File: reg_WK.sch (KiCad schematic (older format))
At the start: 32 parts, among them U36 74HC373, U37 74HC373, U38 74HC244, U39 74HC244, U40 74HC244, U41 74HC244

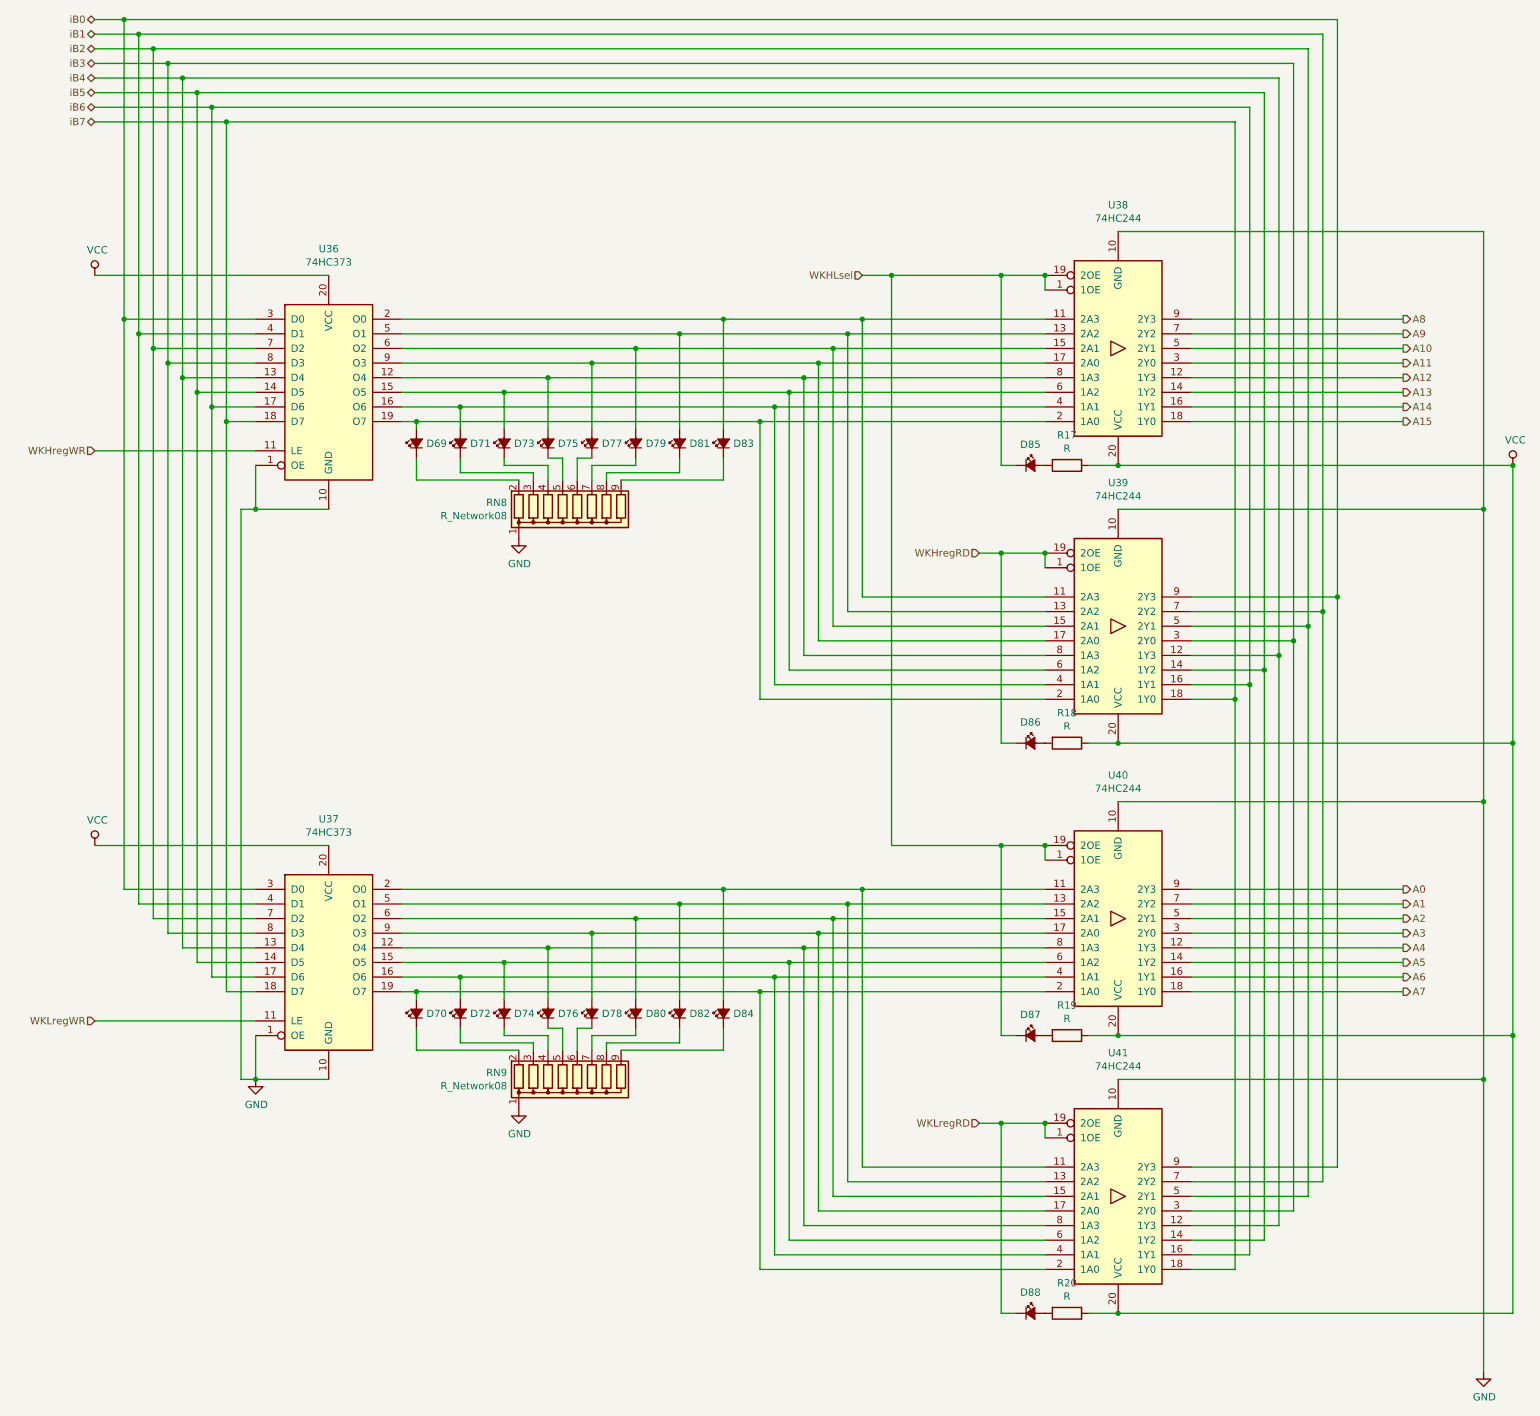
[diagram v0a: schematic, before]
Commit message: placed WKL register, start routing
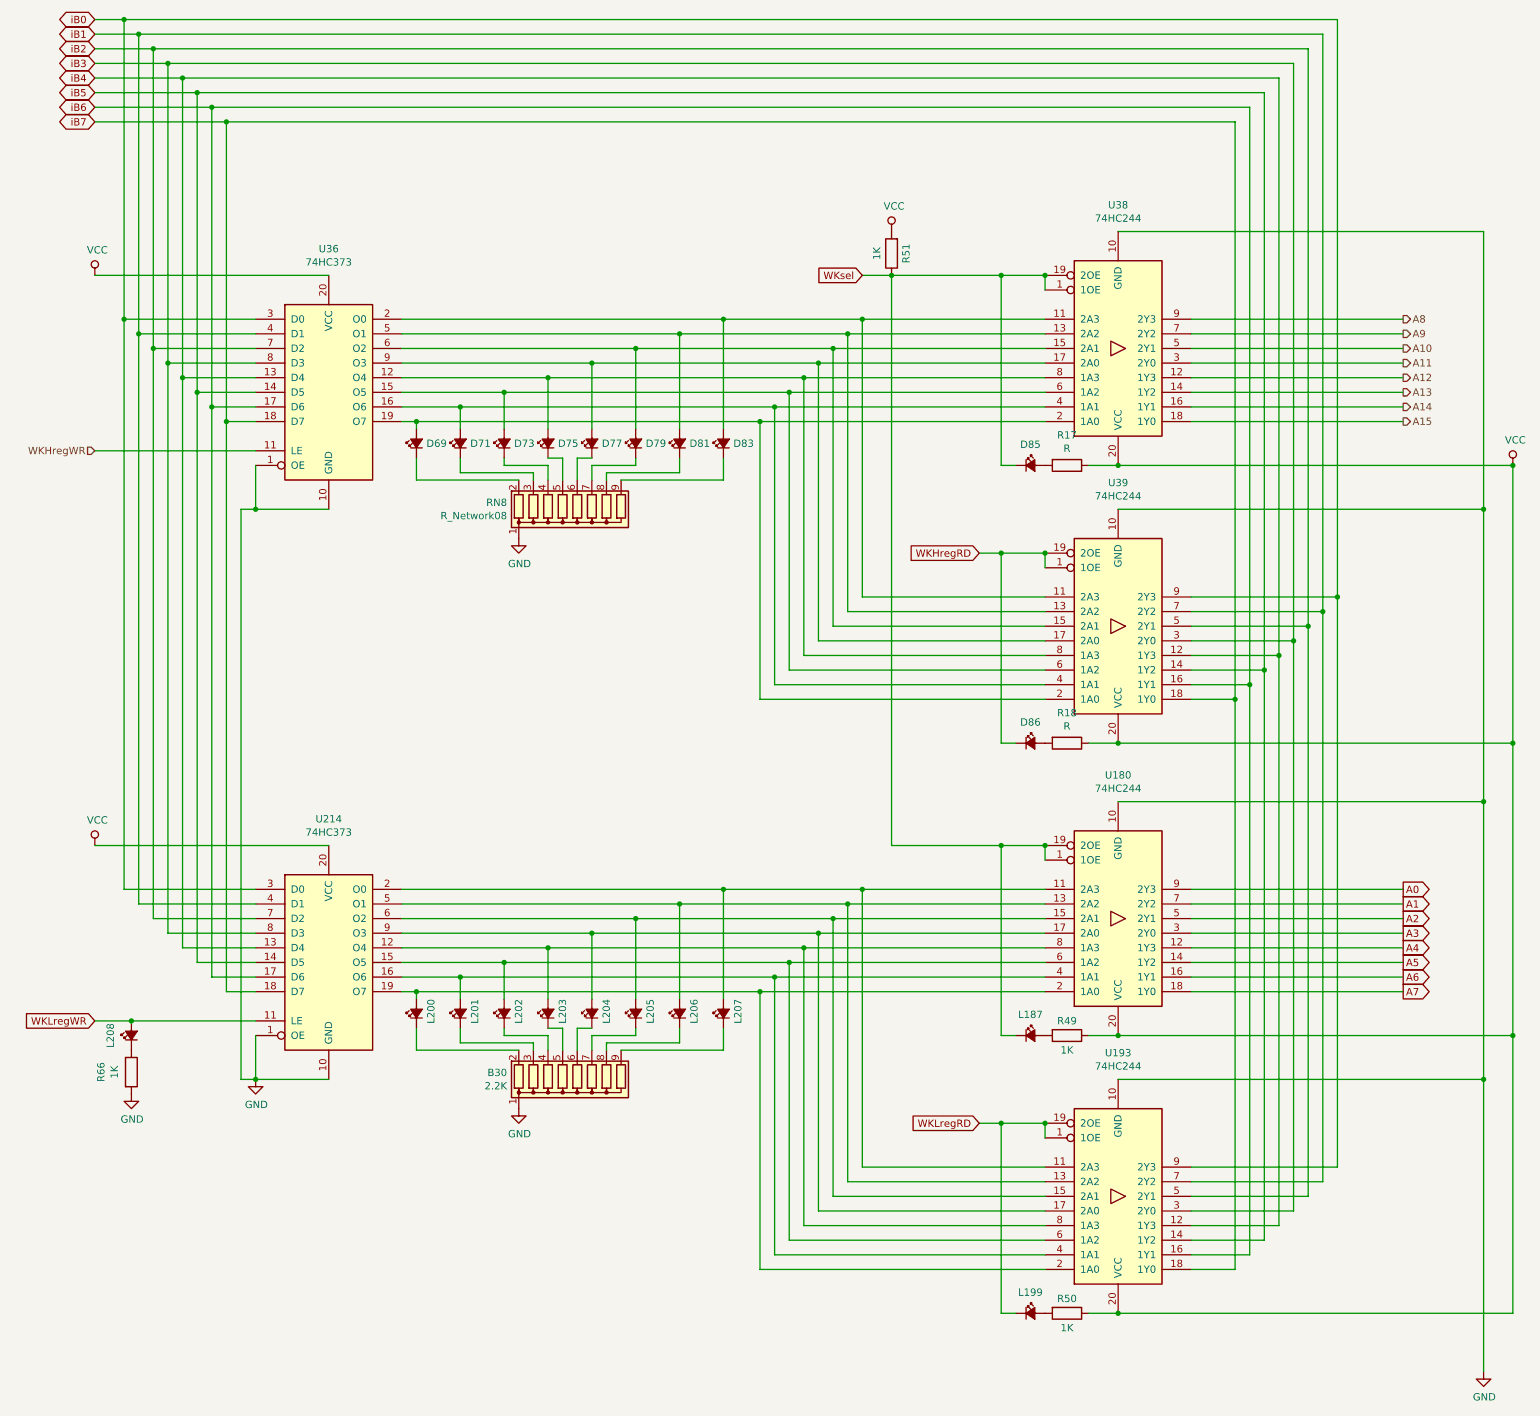
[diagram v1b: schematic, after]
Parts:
- added L208: LED_Small_ALT, LED_THT:LED_D3.0mm, symbol Device:LED_Small_ALT
- added R51, R66: 1K, Resistor_THT:R_Axial_DIN0207_L6.3mm_D2.5mm_P10.16mm_Horizontal, symbol Device:R
- B30: renamed from RN9; value R_Network08 -> 2.2K
- R49: renamed from R19; value R -> 1K
- R50: renamed from R20; value R -> 1K
- renumbered D87 to L187, D88 to L199, D70 to L200, D72 to L201, D74 to L202, D76 to L203, D78 to L204, D80 to L205, D82 to L206, D84 to L207, U40 to U180, U41 to U193, U37 to U214
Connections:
- net GND: now also R66.2
- net VCC: now also R51.2
- net WKLregWR: now also L208.2 (A)
- net WKHLsel renamed WKsel
- net WKsel: now also R51.1
- new net: L208.1 (K), R66.1

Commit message: oops, had to redo part of the PC because I inverted U182 and U195, also routed A0-A7 through the PC register
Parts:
- R49, R50, R51, R66: footprint Resistor_THT:R_Axial_DIN0207_L6.3mm_D2.5mm_P10.16mm_Horizontal -> Resistor_THT:R_Axial_DIN0204_L3.6mm_D1.6mm_P5.08mm_Horizontal
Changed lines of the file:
@@
 F 0 "R49" V 7950 8100 50  0000 C CNN
 F 1 "1K" V 8150 8100 50  0000 C CNN
-F 2 "Resistor_THT:R_Axial_DIN0207_L6.3mm_D2.5mm_P10.16mm_Horizontal" V 7980 8100 50  0001 C CNN
+F 2 "Resistor_THT:R_Axial_DIN0204_L3.6mm_D1.6mm_P5.08mm_Horizontal" V 7980 8100 50  0001 C CNN
 F 3 "~" H 8050 8100 50  0001 C CNN
 	1    8050 8100
@@
 F 0 "R50" V 7950 10000 50  0000 C CNN
 F 1 "1K" V 8150 10000 50  0000 C CNN
-F 2 "Resistor_THT:R_Axial_DIN0207_L6.3mm_D2.5mm_P10.16mm_Horizontal" V 7980 10000 50  0001 C CNN
+F 2 "Resistor_THT:R_Axial_DIN0204_L3.6mm_D1.6mm_P5.08mm_Horizontal" V 7980 10000 50  0001 C CNN
 F 3 "~" H 8050 10000 50  0001 C CNN
 	1    8050 10000
@@
 F 0 "R66" V 1443 8350 50  0000 C CNN
 F 1 "1K" V 1534 8350 50  0000 C CNN
-F 2 "Resistor_THT:R_Axial_DIN0207_L6.3mm_D2.5mm_P10.16mm_Horizontal" V 1580 8350 50  0001 C CNN
+F 2 "Resistor_THT:R_Axial_DIN0204_L3.6mm_D1.6mm_P5.08mm_Horizontal" V 1580 8350 50  0001 C CNN
 F 3 "~" H 1650 8350 50  0001 C CNN
 	1    1650 8350
@@
 P 1650 8500
 AR Path="/5D8315BB/5CFE7E22" Ref="#PWR?"  Part="1"
-AR Path="/5E045D26/5CFE7E22" Ref="#PWR?"  Part="1"
-F 0 "#PWR?" H 1650 8250 50  0001 C CNN
+AR Path="/5E045D26/5CFE7E22" Ref="#PWR0205"  Part="1"
+F 0 "#PWR0205" H 1650 8250 50  0001 C CNN
 F 1 "GND" H 1655 8327 50  0000 C CNN
 F 2 "" H 1650 8500 50  0001 C CNN
@@
 F 0 "R51" V 6750 2750 50  0000 C CNN
 F 1 "1K" V 6950 2750 50  0000 C CNN
-F 2 "Resistor_THT:R_Axial_DIN0207_L6.3mm_D2.5mm_P10.16mm_Horizontal" V 6780 2750 50  0001 C CNN
+F 2 "Resistor_THT:R_Axial_DIN0204_L3.6mm_D1.6mm_P5.08mm_Horizontal" V 6780 2750 50  0001 C CNN
 F 3 "~" H 6850 2750 50  0001 C CNN
 	1    6850 2750
@@
 AR Path="/5D8315BB/5D001AE2" Ref="#PWR?"  Part="1"
 AR Path="/5E031B2C/5D001AE2" Ref="#PWR?"  Part="1"
-AR Path="/5E045D26/5D001AE2" Ref="#PWR?"  Part="1"
-F 0 "#PWR?" H 6850 2450 50  0001 C CNN
+AR Path="/5E045D26/5D001AE2" Ref="#PWR0206"  Part="1"
+F 0 "#PWR0206" H 6850 2450 50  0001 C CNN
 F 1 "VCC" H 6867 2773 50  0000 C CNN
 F 2 "" H 6850 2600 50  0001 C CNN

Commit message: route part of A8-A15 from WKL to WKH
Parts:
- removed D85: LED_Small_ALT, LED_THT:LED_D3.0mm, symbol Device:LED_Small_ALT
- removed R17: R, Resistor_THT:R_Axial_DIN0207_L6.3mm_D2.5mm_P10.16mm_Horizontal, symbol Device:R
- added L198: LED_Small_ALT, LED_THT:LED_D3.0mm, symbol Device:LED_Small_ALT
- added R65: 1K, Resistor_THT:R_Axial_DIN0204_L3.6mm_D1.6mm_P5.08mm_Horizontal, symbol Device:R
- B29: renamed from RN8; value R_Network08 -> 2.2K
- R64: renamed from R18; value R -> 1K; footprint Resistor_THT:R_Axial_DIN0207_L6.3mm_D2.5mm_P10.16mm_Horizontal -> Resistor_THT:R_Axial_DIN0204_L3.6mm_D1.6mm_P5.08mm_Horizontal
- renumbered D86 to L189, D83 to L190, D81 to L191, D79 to L192, D77 to L193, D75 to L194, D73 to L195, D71 to L196, D69 to L197, U38 to U179, U39 to U192, U36 to U213
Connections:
- net GND: now also R65.2
- net WKHregWR: now also L198.2 (A)
- new net: L198.1 (K), R65.1
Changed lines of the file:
@@
 AR Path="/5D8315BB/5E39B533" Ref="U?"  Part="1"
 AR Path="/5E031B2C/5E39B533" Ref="U?"  Part="1"
-AR Path="/5E045D26/5E39B533" Ref="U36"  Part="1"
-F 0 "U36" H 3000 4681 50  0000 C CNN
+AR Path="/5E045D26/5E39B533" Ref="U213"  Part="1"
+F 0 "U213" H 3000 4681 50  0000 C CNN
 F 1 "74HC373" H 3000 4590 50  0000 C CNN
 F 2 "Package_DIP:DIP-20_W7.62mm" H 3000 3700 50  0001 C CNN
@@
 	1    0    0    -1
 $EndComp
-Text HLabel 1400 4100 0    50   Input ~ 0
-WKHregWR
 $Comp
 L Device:LED_Small_ALT D?
@@
 AR Path="/5D8315BB/5E39B55B" Ref="D?"  Part="1"
 AR Path="/5E031B2C/5E39B55B" Ref="D?"  Part="1"
-AR Path="/5E045D26/5E39B55B" Ref="D69"  Part="1"
-F 0 "D69" V 3600 3982 50  0000 R CNN
+AR Path="/5E045D26/5E39B55B" Ref="L197"  Part="1"
+F 0 "L197" V 3600 3982 50  0000 R CNN
 F 1 "LED_Small_ALT" V 3555 3982 50  0001 R CNN
 F 2 "LED_THT:LED_D3.0mm" V 3600 4050 50  0001 C CNN
@@
 AR Path="/5D8315BB/5E39B561" Ref="D?"  Part="1"
 AR Path="/5E031B2C/5E39B561" Ref="D?"  Part="1"
-AR Path="/5E045D26/5E39B561" Ref="D71"  Part="1"
-F 0 "D71" V 3900 3982 50  0000 R CNN
+AR Path="/5E045D26/5E39B561" Ref="L196"  Part="1"
+F 0 "L196" V 3900 3982 50  0000 R CNN
 F 1 "LED_Small_ALT" V 3855 3982 50  0001 R CNN
 F 2 "LED_THT:LED_D3.0mm" V 3900 4050 50  0001 C CNN
@@
 AR Path="/5D8315BB/5E39B567" Ref="D?"  Part="1"
 AR Path="/5E031B2C/5E39B567" Ref="D?"  Part="1"
-AR Path="/5E045D26/5E39B567" Ref="D73"  Part="1"
-F 0 "D73" V 4200 3982 50  0000 R CNN
+AR Path="/5E045D26/5E39B567" Ref="L195"  Part="1"
+F 0 "L195" V 4200 3982 50  0000 R CNN
 F 1 "LED_Small_ALT" V 4155 3982 50  0001 R CNN
 F 2 "LED_THT:LED_D3.0mm" V 4200 4050 50  0001 C CNN
@@
 AR Path="/5D8315BB/5E39B56D" Ref="D?"  Part="1"
 AR Path="/5E031B2C/5E39B56D" Ref="D?"  Part="1"
-AR Path="/5E045D26/5E39B56D" Ref="D75"  Part="1"
-F 0 "D75" V 4500 3982 50  0000 R CNN
+AR Path="/5E045D26/5E39B56D" Ref="L194"  Part="1"
+F 0 "L194" V 4500 3982 50  0000 R CNN
 F 1 "LED_Small_ALT" V 4455 3982 50  0001 R CNN
 F 2 "LED_THT:LED_D3.0mm" V 4500 4050 50  0001 C CNN
@@
 AR Path="/5D8315BB/5E39B573" Ref="D?"  Part="1"
 AR Path="/5E031B2C/5E39B573" Ref="D?"  Part="1"
-AR Path="/5E045D26/5E39B573" Ref="D77"  Part="1"
-F 0 "D77" V 4800 3982 50  0000 R CNN
+AR Path="/5E045D26/5E39B573" Ref="L193"  Part="1"
+F 0 "L193" V 4800 3982 50  0000 R CNN
 F 1 "LED_Small_ALT" V 4755 3982 50  0001 R CNN
 F 2 "LED_THT:LED_D3.0mm" V 4800 4050 50  0001 C CNN
@@
 AR Path="/5D8315BB/5E39B579" Ref="D?"  Part="1"
 AR Path="/5E031B2C/5E39B579" Ref="D?"  Part="1"
-AR Path="/5E045D26/5E39B579" Ref="D79"  Part="1"
-F 0 "D79" V 5100 3982 50  0000 R CNN
+AR Path="/5E045D26/5E39B579" Ref="L192"  Part="1"
+F 0 "L192" V 5100 3982 50  0000 R CNN
 F 1 "LED_Small_ALT" V 5055 3982 50  0001 R CNN
 F 2 "LED_THT:LED_D3.0mm" V 5100 4050 50  0001 C CNN
@@
 AR Path="/5D8315BB/5E39B57F" Ref="D?"  Part="1"
 AR Path="/5E031B2C/5E39B57F" Ref="D?"  Part="1"
-AR Path="/5E045D26/5E39B57F" Ref="D81"  Part="1"
-F 0 "D81" V 5400 3982 50  0000 R CNN
+AR Path="/5E045D26/5E39B57F" Ref="L191"  Part="1"
+F 0 "L191" V 5400 3982 50  0000 R CNN
 F 1 "LED_Small_ALT" V 5355 3982 50  0001 R CNN
 F 2 "LED_THT:LED_D3.0mm" V 5400 4050 50  0001 C CNN
@@
 AR Path="/5D8315BB/5E39B585" Ref="D?"  Part="1"
 AR Path="/5E031B2C/5E39B585" Ref="D?"  Part="1"
-AR Path="/5E045D26/5E39B585" Ref="D83"  Part="1"
-F 0 "D83" V 5700 3982 50  0000 R CNN
+AR Path="/5E045D26/5E39B585" Ref="L190"  Part="1"
+F 0 "L190" V 5700 3982 50  0000 R CNN
 F 1 "LED_Small_ALT" V 5655 3982 50  0001 R CNN
 F 2 "LED_THT:LED_D3.0mm" V 5700 4050 50  0001 C CNN
@@
 AR Path="/5D8315BB/5E39B58B" Ref="RN?"  Part="1"
 AR Path="/5E031B2C/5E39B58B" Ref="RN?"  Part="1"
-AR Path="/5E045D26/5E39B58B" Ref="RN8"  Part="1"
-F 0 "RN8" H 4220 4454 50  0000 R CNN
-F 1 "R_Network08" H 4220 4545 50  0000 R CNN
+AR Path="/5E045D26/5E39B58B" Ref="B29"  Part="1"
+F 0 "B29" H 4220 4454 50  0000 R CNN
+F 1 "2.2K" H 4220 4545 50  0000 R CNN
 F 2 "Resistor_THT:R_Array_SIP9" V 5175 4500 50  0001 C CNN
 F 3 "http://www.vishay.com/docs/31509/csc.pdf" H 4700 4500 50  0001 C CNN
@@
 AR Path="/5D8315BB/5E39B5BB" Ref="U?"  Part="1"
 AR Path="/5E031B2C/5E39B5BB" Ref="U?"  Part="1"
-AR Path="/5E045D26/5E39B5BB" Ref="U38"  Part="1"
-F 0 "U38" H 8400 2419 50  0000 C CNN
+AR Path="/5E045D26/5E39B5BB" Ref="U179"  Part="1"
+F 0 "U179" H 8400 2419 50  0000 C CNN
 F 1 "74HC244" H 8400 2510 50  0000 C CNN
 F 2 "Package_DIP:DIP-20_W7.62mm" H 8400 3400 50  0001 C CNN
@@
 Connection ~ 7900 2900
 $Comp
-L Device:R R?
-U 1 1 5E39B5CB
-P 8050 4200
-AR Path="/5CAD6F89/5E39B5CB" Ref="R?"  Part="1"
-AR Path="/5D8315BB/5E39B5CB" Ref="R?"  Part="1"
-AR Path="/5E031B2C/5E39B5CB" Ref="R?"  Part="1"
-AR Path="/5E045D26/5E39B5CB" Ref="R17"  Part="1"
-F 0 "R17" V 7843 4200 50  0000 C CNN
-F 1 "R" V 7934 4200 50  0000 C CNN
-F 2 "Resistor_THT:R_Axial_DIN0207_L6.3mm_D2.5mm_P10.16mm_Horizontal" V 7980 4200 50  0001 C CNN
-F 3 "~" H 8050 4200 50  0001 C CNN
-	1    8050 4200
-	0    1    1    0
-$EndComp
-$Comp
-L Device:LED_Small_ALT D?
-U 1 1 5E39B5D1
-P 7800 4200
-AR Path="/5CAD6F89/5E39B5D1" Ref="D?"  Part="1"
-AR Path="/5D8315BB/5E39B5D1" Ref="D?"  Part="1"
-AR Path="/5E031B2C/5E39B5D1" Ref="D?"  Part="1"
-AR Path="/5E045D26/5E39B5D1" Ref="D85"  Part="1"
-F 0 "D85" H 7800 4343 50  0000 C CNN
-F 1 "LED_Small_ALT" V 7755 4132 50  0001 R CNN
-F 2 "LED_THT:LED_D3.0mm" V 7800 4200 50  0001 C CNN
-F 3 "~" V 7800 4200 50  0001 C CNN
-	1    7800 4200
-	1    0    0    -1
-$EndComp
-$Comp
 L 74xx:74HC244 U?
 U 1 1 5E39B5D8
@@
 AR Path="/5D8315BB/5E39B5D8" Ref="U?"  Part="1"
 AR Path="/5E031B2C/5E39B5D8" Ref="U?"  Part="1"
-AR Path="/5E045D26/5E39B5D8" Ref="U39"  Part="1"
-F 0 "U39" H 8400 4319 50  0000 C CNN
+AR Path="/5E045D26/5E39B5D8" Ref="U192"  Part="1"
+F 0 "U192" H 8400 4319 50  0000 C CNN
 F 1 "74HC244" H 8400 4410 50  0000 C CNN
 F 2 "Package_DIP:DIP-20_W7.62mm" H 8400 5300 50  0001 C CNN
@@
 Wire Wire Line
 	8900 7800 10350 7800
-Text HLabel 10350 3200 2    50   Output ~ 0
-A8
-Text HLabel 10350 3300 2    50   Output ~ 0
-A9
-Text HLabel 10350 3400 2    50   Output ~ 0
-A10
-Text HLabel 10350 3500 2    50   Output ~ 0
-A11
-Text HLabel 10350 3600 2    50   Output ~ 0
-A12
-Text HLabel 10350 3700 2    50   Output ~ 0
-A13
-Text HLabel 10350 3800 2    50   Output ~ 0
-A14
-Text HLabel 10350 3900 2    50   Output ~ 0
-A15
 Wire Wire Line
 	8400 4200 11100 4200
@@
 Wire Wire Line
 	10900 4500 10900 6500
-Wire Wire Line
-	6850 2900 7600 2900
-Wire Wire Line
-	7700 4200 7600 4200
-Wire Wire Line
-	7600 4200 7600 2900
-Connection ~ 7600 2900
-Wire Wire Line
-	7600 2900 7900 2900
-Wire Wire Line
-	8200 4200 8400 4200
-Connection ~ 8400 4200
 Wire Wire Line
 	7450 4800 7600 4800
@@
 AR Path="/5D8315BB/5E39B75F" Ref="R?"  Part="1"
 AR Path="/5E031B2C/5E39B75F" Ref="R?"  Part="1"
-AR Path="/5E045D26/5E39B75F" Ref="R18"  Part="1"
-F 0 "R18" V 7843 6100 50  0000 C CNN
-F 1 "R" V 7934 6100 50  0000 C CNN
-F 2 "Resistor_THT:R_Axial_DIN0207_L6.3mm_D2.5mm_P10.16mm_Horizontal" V 7980 6100 50  0001 C CNN
+AR Path="/5E045D26/5E39B75F" Ref="R64"  Part="1"
+F 0 "R64" V 7843 6100 50  0000 C CNN
+F 1 "1K" V 7934 6100 50  0000 C CNN
+F 2 "Resistor_THT:R_Axial_DIN0204_L3.6mm_D1.6mm_P5.08mm_Horizontal" V 7980 6100 50  0001 C CNN
 F 3 "~" H 8050 6100 50  0001 C CNN
 	1    8050 6100
@@
 AR Path="/5D8315BB/5E39B765" Ref="D?"  Part="1"
 AR Path="/5E031B2C/5E39B765" Ref="D?"  Part="1"
-AR Path="/5E045D26/5E39B765" Ref="D86"  Part="1"
-F 0 "D86" H 7800 6243 50  0000 C CNN
+AR Path="/5E045D26/5E39B765" Ref="L189"  Part="1"
+F 0 "L189" H 7800 6243 50  0000 C CNN
 F 1 "LED_Small_ALT" V 7755 6032 50  0001 R CNN
 F 2 "LED_THT:LED_D3.0mm" V 7800 6100 50  0001 C CNN
@@
 $EndComp
 Wire Wire Line
-	1400 4100 2500 4100
+	1400 4100 1450 4100
 Text GLabel 1400 8000 0    50   Input ~ 0
 WKLregWR
@@
 Text GLabel 10350 7800 2    50   Output ~ 0
 A7
+Text GLabel 1400 4100 0    50   Input ~ 0
+WKHregWR
+$Comp
+L Device:R R?
+U 1 1 5CFC7103
+P 1450 4600
+AR Path="/5CAD6F89/5CFC7103" Ref="R?"  Part="1"
+AR Path="/5D8315BB/5CFC7103" Ref="R?"  Part="1"
+AR Path="/5E031B2C/5CFC7103" Ref="R?"  Part="1"
+AR Path="/5E045D26/5CFC7103" Ref="R65"  Part="1"
+F 0 "R65" V 1243 4600 50  0000 C CNN
+F 1 "1K" V 1334 4600 50  0000 C CNN
+F 2 "Resistor_THT:R_Axial_DIN0204_L3.6mm_D1.6mm_P5.08mm_Horizontal" V 1380 4600 50  0001 C CNN
+F 3 "~" H 1450 4600 50  0001 C CNN
+	1    1450 4600
+	1    0    0    -1
+$EndComp
+$Comp
+L Device:LED_Small_ALT D?
+U 1 1 5CFC7109
+P 1450 4350
+AR Path="/5CAD6F89/5CFC7109" Ref="D?"  Part="1"
+AR Path="/5D8315BB/5CFC7109" Ref="D?"  Part="1"
+AR Path="/5E031B2C/5CFC7109" Ref="D?"  Part="1"
+AR Path="/5E045D26/5CFC7109" Ref="L198"  Part="1"
+F 0 "L198" H 1450 4493 50  0000 C CNN
+F 1 "LED_Small_ALT" V 1405 4282 50  0001 R CNN
+F 2 "LED_THT:LED_D3.0mm" V 1450 4350 50  0001 C CNN
+F 3 "~" V 1450 4350 50  0001 C CNN
+	1    1450 4350
+	0    -1   -1   0
+$EndComp
+$Comp
+L power:GND #PWR?
+U 1 1 5CFC710F
+P 1450 4750
+AR Path="/5D8315BB/5CFC710F" Ref="#PWR?"  Part="1"
+AR Path="/5E045D26/5CFC710F" Ref="#PWR0207"  Part="1"
+F 0 "#PWR0207" H 1450 4500 50  0001 C CNN
+F 1 "GND" H 1455 4577 50  0000 C CNN
+F 2 "" H 1450 4750 50  0001 C CNN
+F 3 "" H 1450 4750 50  0001 C CNN
+	1    1450 4750
+	1    0    0    -1
+$EndComp
+Wire Wire Line
+	1450 4250 1450 4100
+Connection ~ 1450 4100
+Wire Wire Line
+	1450 4100 2500 4100
+Wire Wire Line
+	6850 2900 7900 2900
+Text GLabel 10350 3200 2    50   Output ~ 0
+A8
+Text GLabel 10350 3300 2    50   Output ~ 0
+A9
+Text GLabel 10350 3400 2    50   Output ~ 0
+A10
+Text GLabel 10350 3500 2    50   Output ~ 0
+A11
+Text GLabel 10350 3600 2    50   Output ~ 0
+A12
+Text GLabel 10350 3700 2    50   Output ~ 0
+A13
+Text GLabel 10350 3800 2    50   Output ~ 0
+A14
+Text GLabel 10350 3900 2    50   Output ~ 0
+A15
 $EndSCHEMATC
